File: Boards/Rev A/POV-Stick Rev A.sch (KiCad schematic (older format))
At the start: 23 parts, among them J1 ISP_Header, J3 Batt Conn, SW1 Power Switch, U1 ATTINY85-20SU, U2 APA102-2020

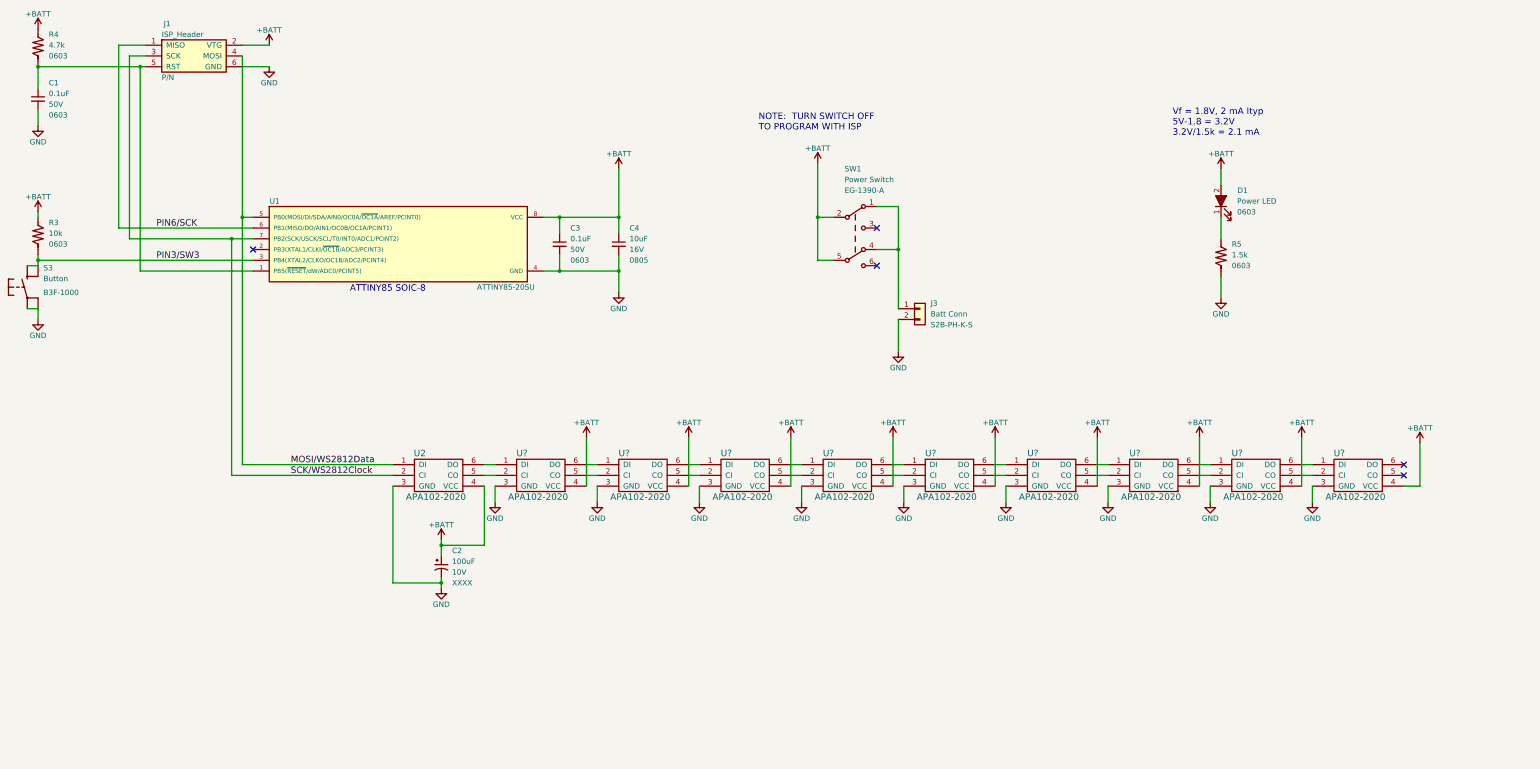
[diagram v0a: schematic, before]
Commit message: Updated APA102-2020 pin numbers
Also changed drawing title block.
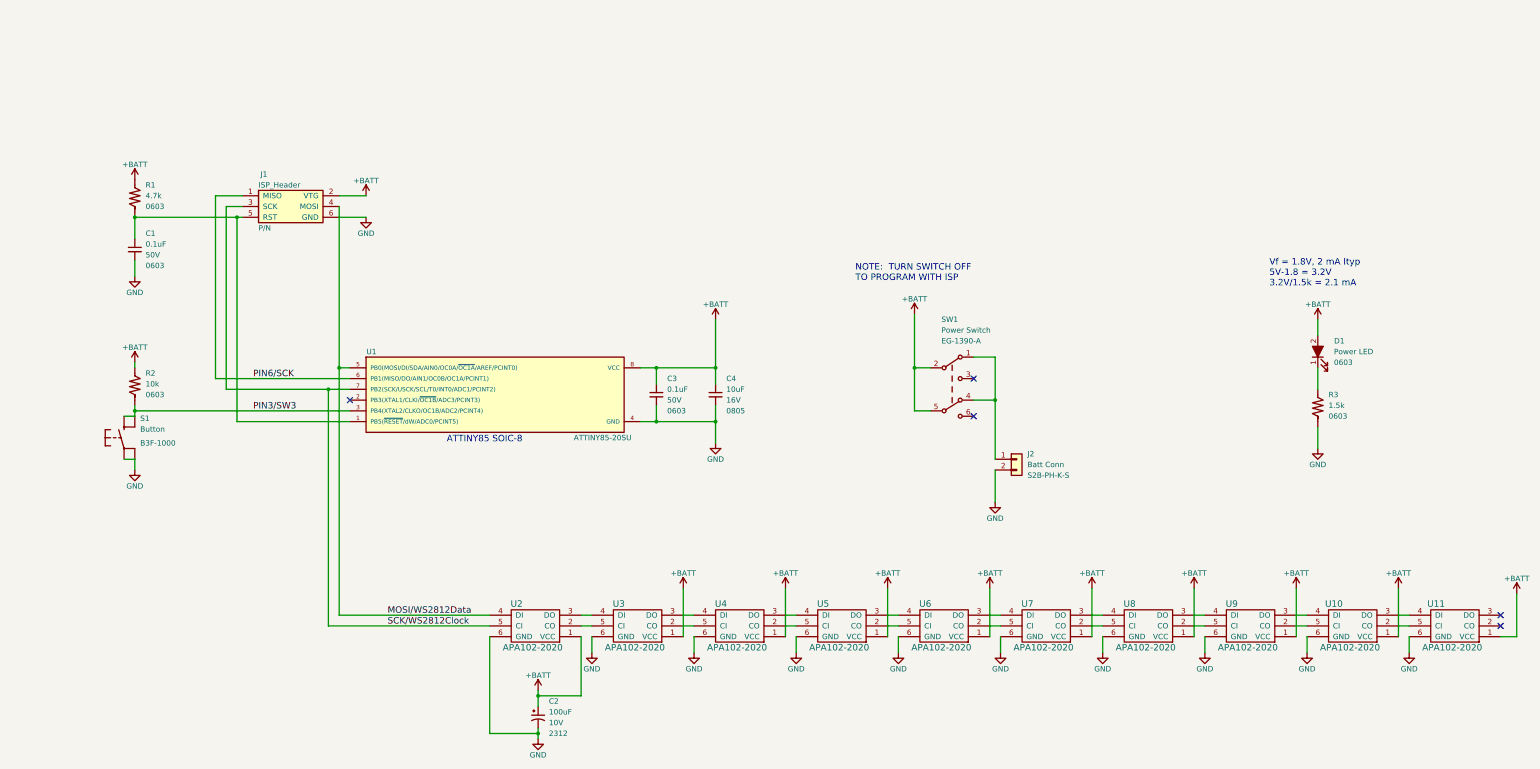
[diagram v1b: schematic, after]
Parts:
- removed U2, U? (x9): APA102-2020, symbol APA102C
- added U10, U11, U2, U3, U4, U5, U6, U7, U8, U9: APA102-2020, symbol APA102-2020
- C2: Package Size XXXX -> 2312
- renumbered J3 to J2, R4 to R1, R3 to R2, R5 to R3, S3 to S1
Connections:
- net +BATT: now also U10.1 (VCC), U11.1 (VCC), U2.1 (VCC), U3.1 (VCC), U4.1 (VCC), U5.1 (VCC), U6.1 (VCC), U7.1 (VCC), U8.1 (VCC), U9.1 (VCC)
- net GND: now also U10.6 (GND), U11.6 (GND), U2.6 (GND), U3.6 (GND), U4.6 (GND), U5.6 (GND), U6.6 (GND), U7.6 (GND), U8.6 (GND), U9.6 (GND)
- net MOSI/WS2812Data: now also U2.4 (DI)
- net SCK/WS2812Clock: now also U2.5 (CI)
- new net: U2.2 (CO), U3.5 (CI)
- new net: U2.3 (DO), U3.4 (DI)
- new net: U3.2 (CO), U4.5 (CI)
- new net: U3.3 (DO), U4.4 (DI)
- new net: U4.2 (CO), U5.5 (CI)
- new net: U4.3 (DO), U5.4 (DI)
- new net: U5.2 (CO), U6.5 (CI)
- new net: U5.3 (DO), U6.4 (DI)
- new net: U6.2 (CO), U7.5 (CI)
- new net: U6.3 (DO), U7.4 (DI)
- new net: U7.2 (CO), U8.5 (CI)
- new net: U7.3 (DO), U8.4 (DI)
- new net: U8.2 (CO), U9.5 (CI)
- new net: U8.3 (DO), U9.4 (DI)
- new net: U10.5 (CI), U9.2 (CO)
- new net: U10.4 (DI), U9.3 (DO)
- new net: U10.2 (CO), U11.5 (CI)
- new net: U10.3 (DO), U11.4 (DI)
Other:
- moved on the sheet: C1, C2, C3, C4, D1, J1, J2, R1, R2, R3, S1, SW1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

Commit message: Added MFR P/Ns
Added MFR P/Ns to all components.
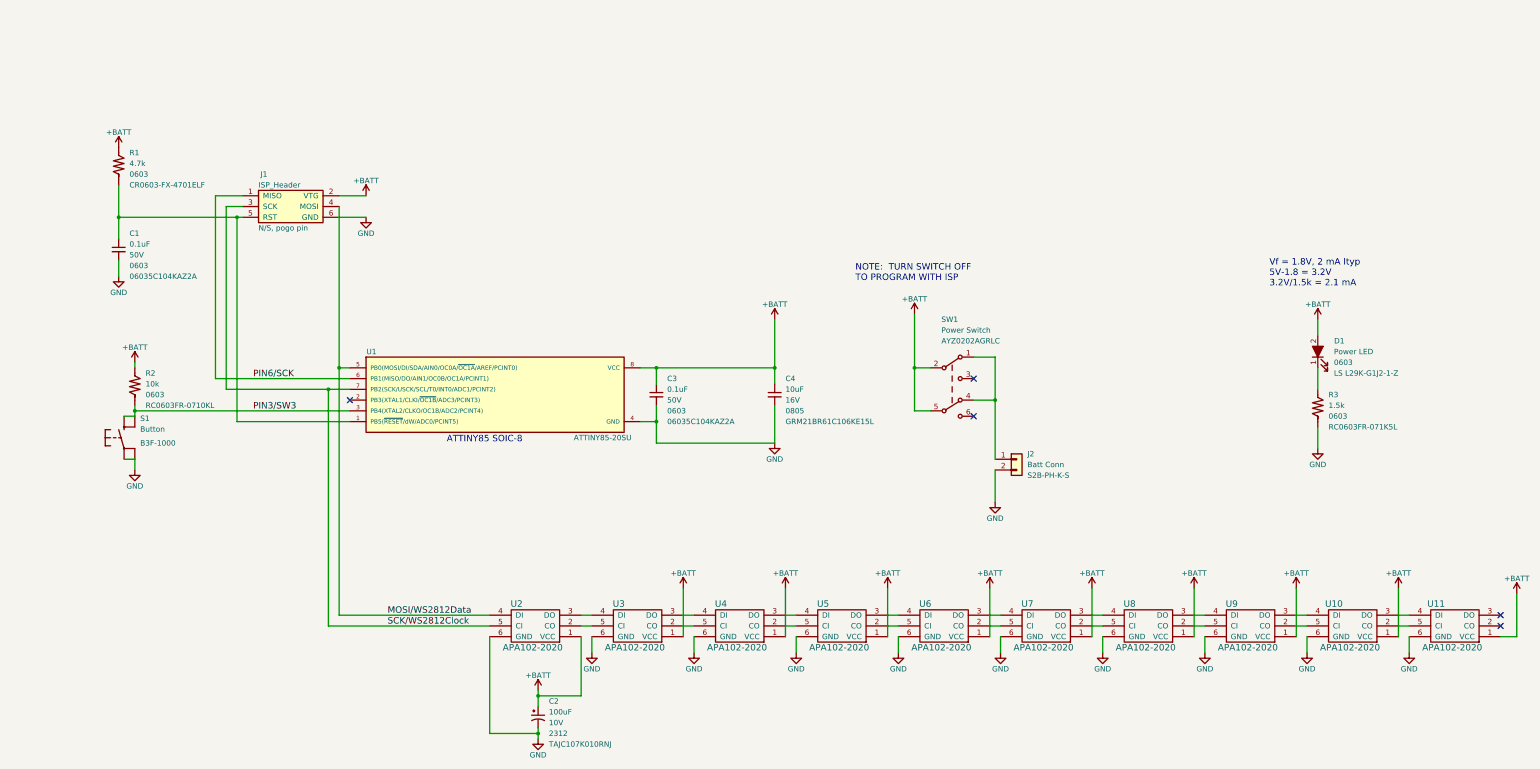
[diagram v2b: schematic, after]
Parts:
- C1, C3: MFR P/N (none) -> 06035C104KAZ2A
- C2: MFR P/N (none) -> TAJC107K010RNJ
- C4: MFR P/N (none) -> GRM21BR61C106KE15L
- D1: MFR P/N (none) -> LS L29K-G1J2-1-Z
- J1: PN P/N -> N/S, pogo pin
- R1: MFR P/N (none) -> CR0603-FX-4701ELF
- R2: MFR P/N (none) -> RC0603FR-0710KL
- R3: Field4 0603 -> (none); MFR P/N (none) -> RC0603FR-071K5L; Package Size (none) -> 0603
- SW1: Part Number EG-1390-A -> AYZ0202AGRLC
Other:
- moved on the sheet: C1, C4, R1

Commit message: Need to add footprints in the schematic editor
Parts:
- SW1: footprint MyFP_Switches:E-Switch_EG1390 -> (none)
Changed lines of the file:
@@
 F 0 "SW1" H 9400 4550 50  0000 L CNN
 F 1 "Power Switch" H 9400 4450 50  0000 L CNN
-F 2 "MyFP_Switches:E-Switch_EG1390" H 9525 4125 50  0001 C CNN
+F 2 "" H 9525 4125 50  0001 C CNN
 F 3 "" H 9525 4125 50  0001 C CNN
 F 4 "AYZ0202AGRLC" H 9400 4350 50  0000 L CNN "Part Number"
